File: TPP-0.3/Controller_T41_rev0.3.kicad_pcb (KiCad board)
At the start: 2 copper layers, 102.9 x 69.9 mm, 56 parts, among them J1 8P8C_x4, J2 8P8C_x4, J3 Screw_Terminal_01x02, J4 RJ45_LED, J5 5v Conn, U1 Teensy4.1, U2 AMS1117-5.0, U3 74HCT245, U4 74HCT245, U5 74HCT245, U6 74HCT245

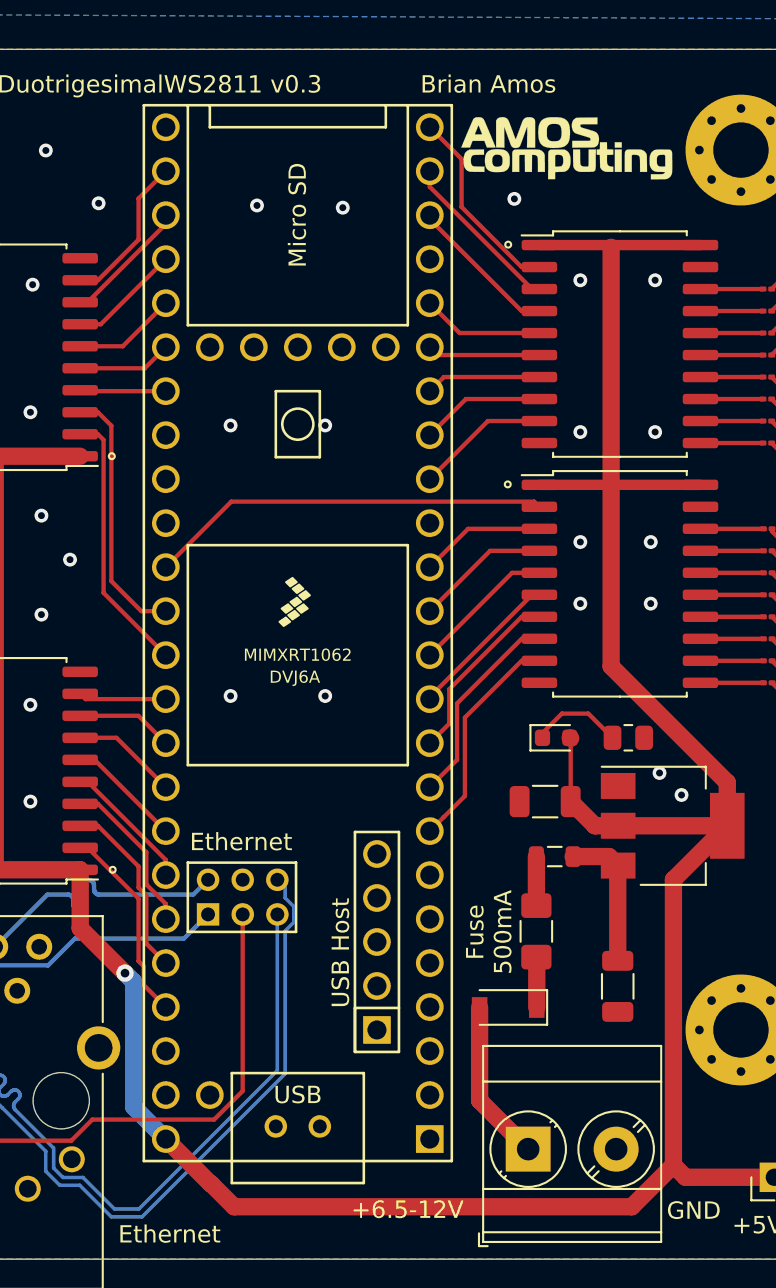
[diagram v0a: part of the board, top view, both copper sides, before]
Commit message: Updated rev0.3 to KiCad 6
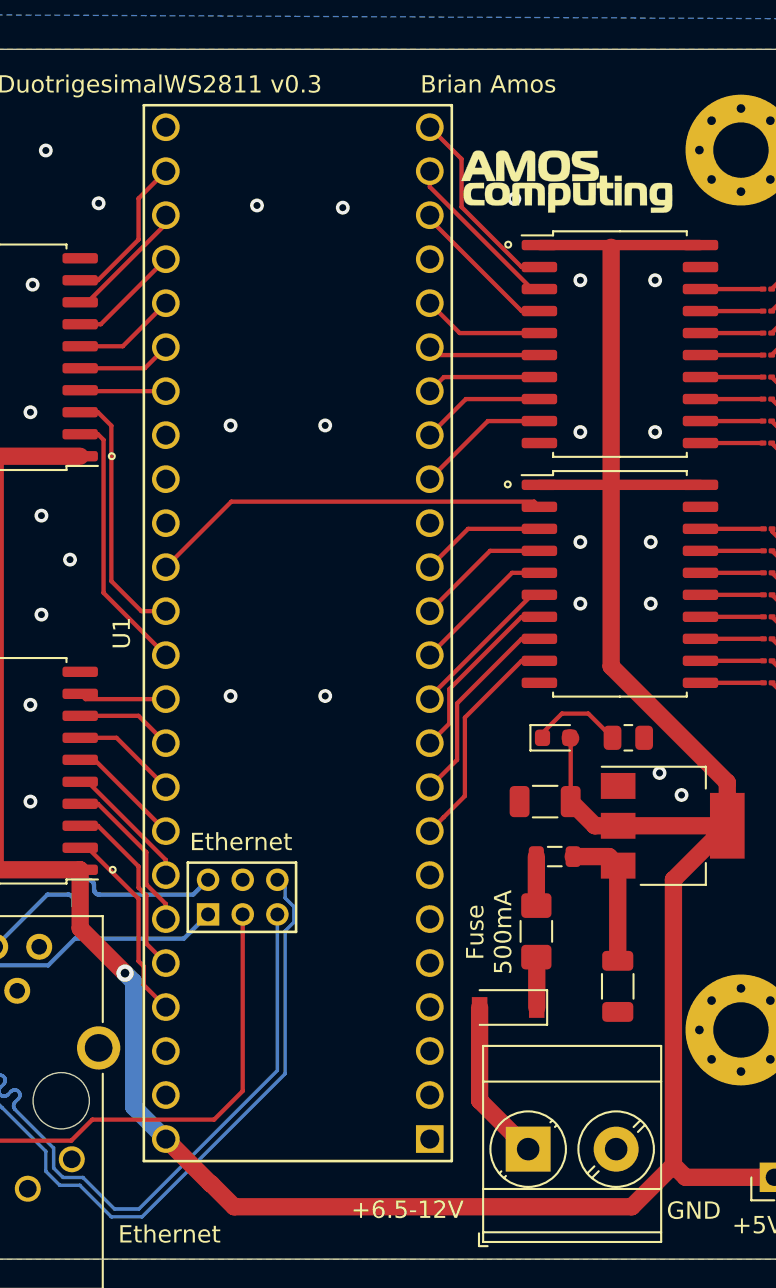
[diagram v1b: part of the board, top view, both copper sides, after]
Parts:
- U1: footprint teensy:Teensy41 -> Teensy:Teensy41-withEthernet
- moved G*** 1.93 mm to (164.4, 58.4)
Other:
- net class Default removed
